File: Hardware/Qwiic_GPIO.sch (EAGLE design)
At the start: 26 parts, among them J2 SMD, J3 PTH, J4 SMD, U3 TCA9534U

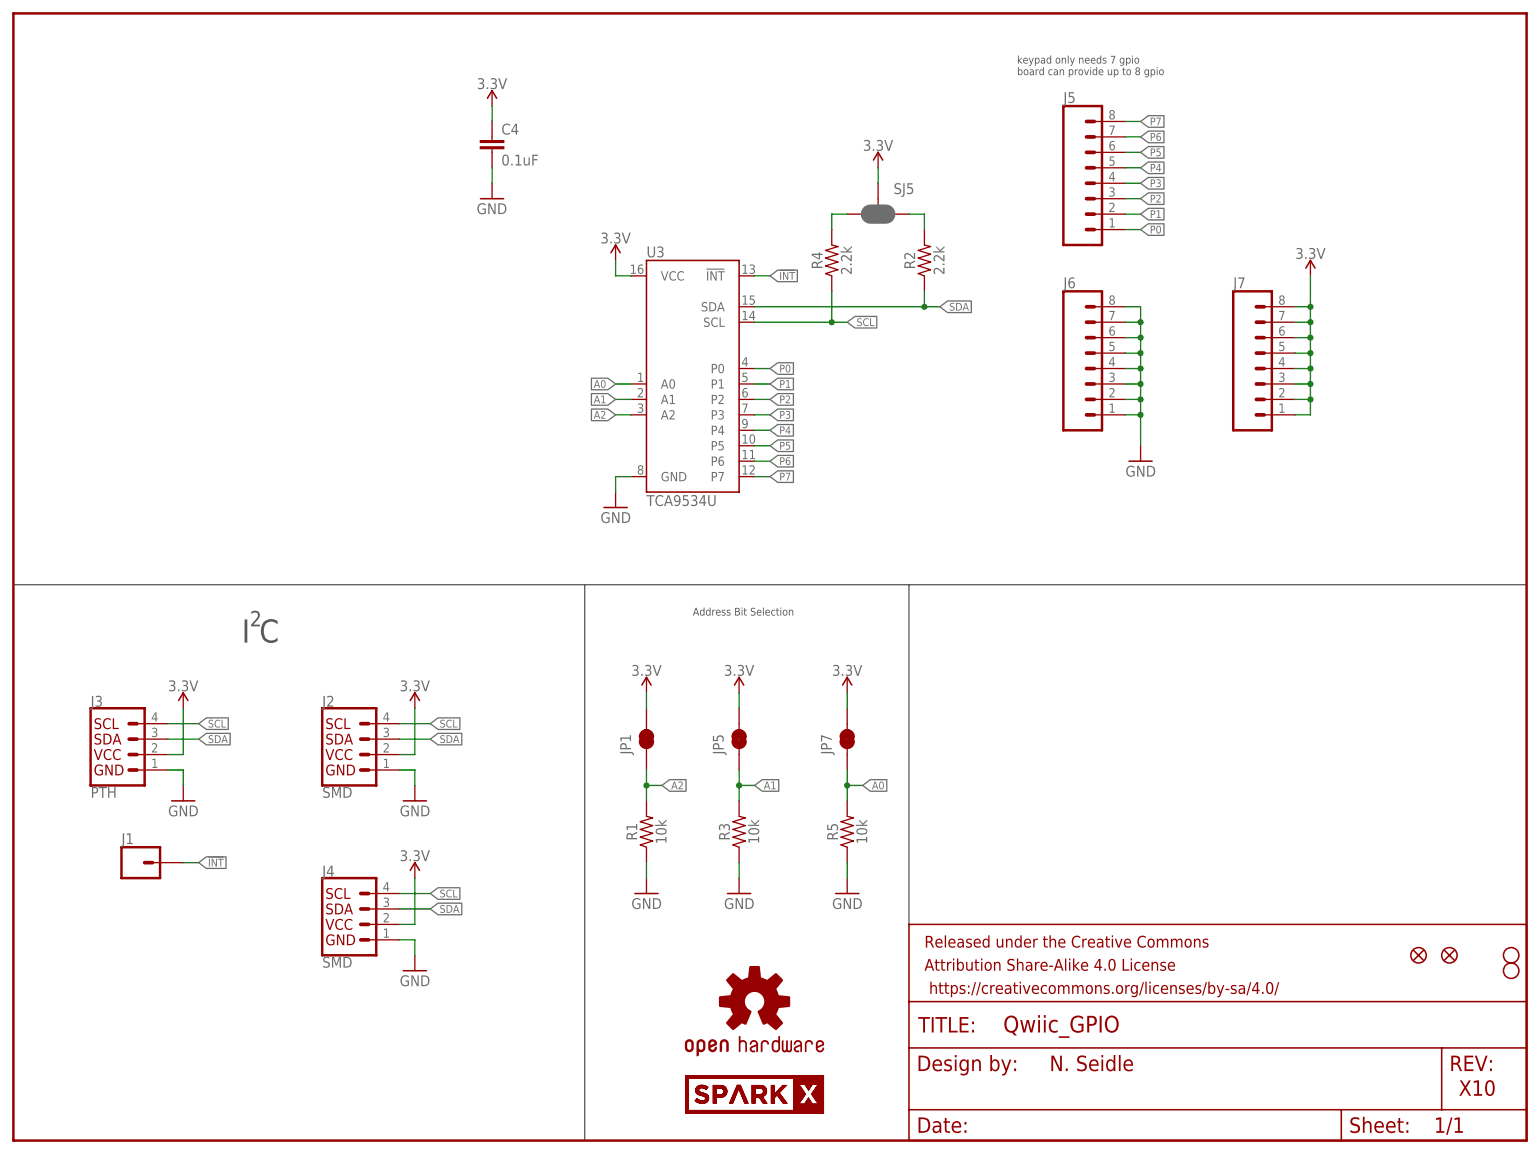
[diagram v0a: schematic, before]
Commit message: added addresses
cleaned up schematic and added addresses.
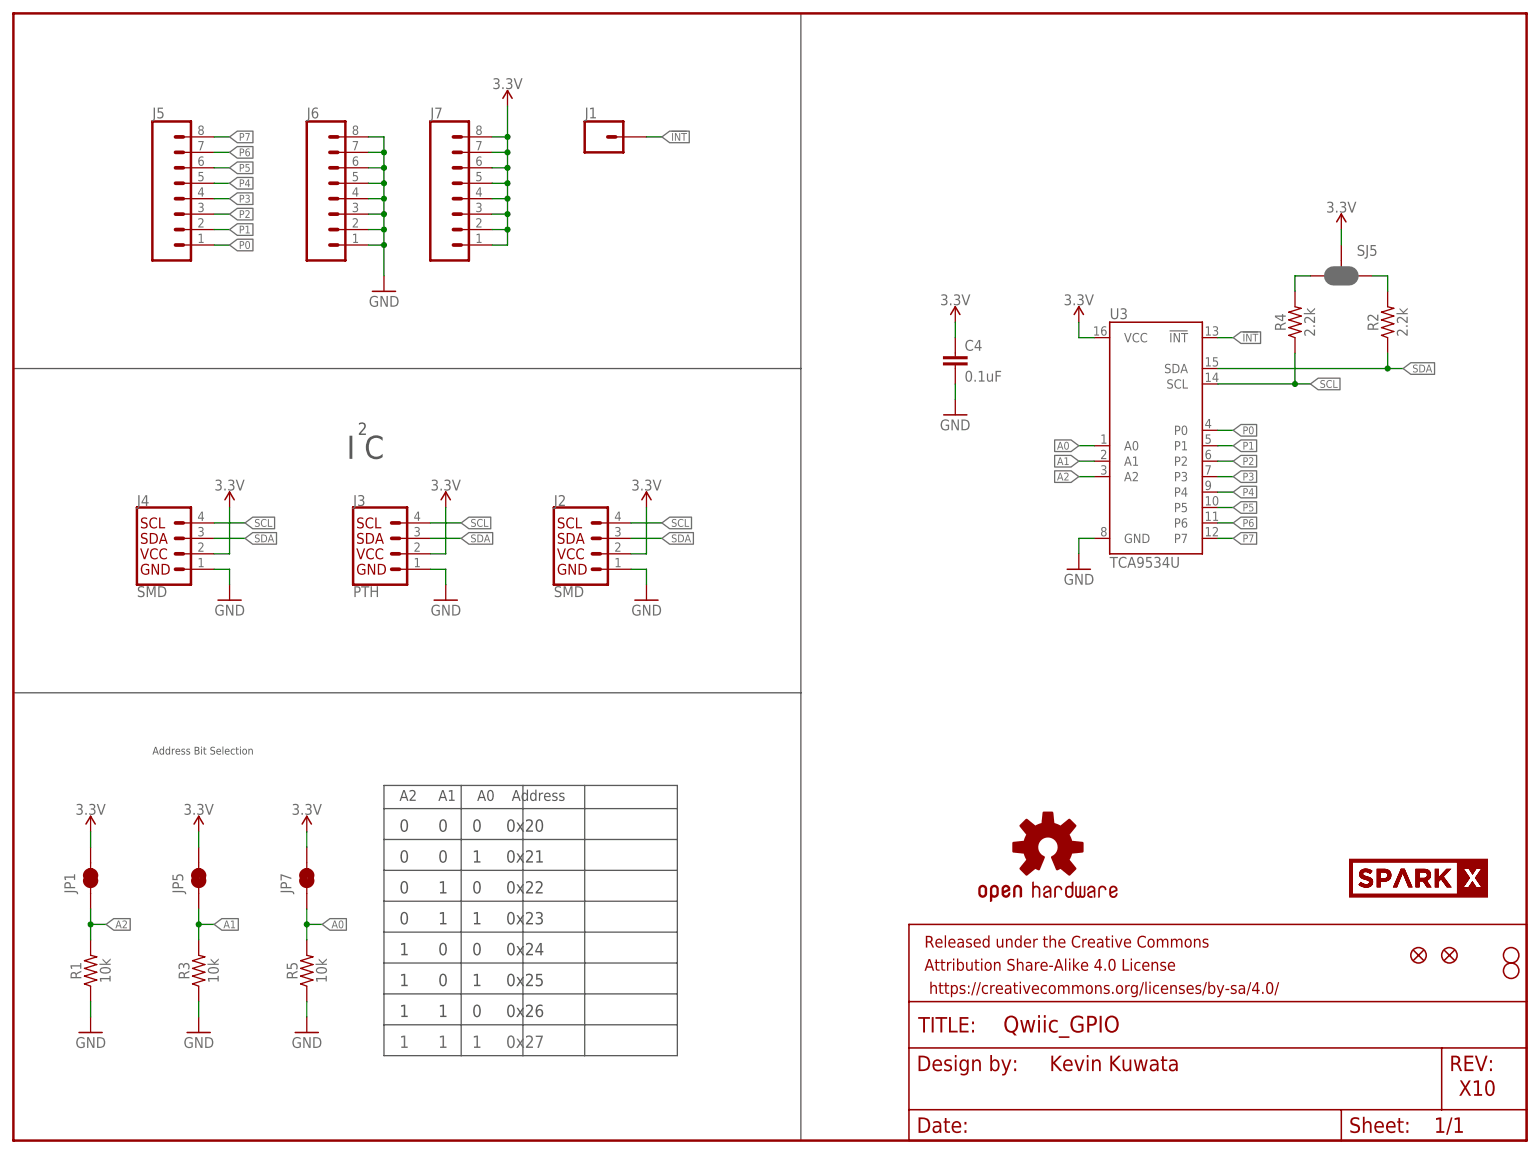
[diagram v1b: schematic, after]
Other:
- note added: "0 0 0 0x20"
- note added: "0 0 1 0x21"
- note added: "0 1 0 0x22"
- note added: "0 1 1 0x23"
- note added: "1 0 0 0x24"
- note added: "1 0 1 0x25"
- note added: "1 1 0 0x26"
- note added: "1 1 1 0x27"
- note added: "A2 A1 A0 Address"
- note added: "Kevin Kuwata"
- note removed: "N. Seidle"
- note removed: "keypad only needs 7 gpio board can provide up to 8 gpio"
- moved on the sheet: C4, J1, J2, J3, J4, J5, J6, J7, JP1, JP5, JP7, R1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

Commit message: Updated PCB with latch terminals and buzzard labels
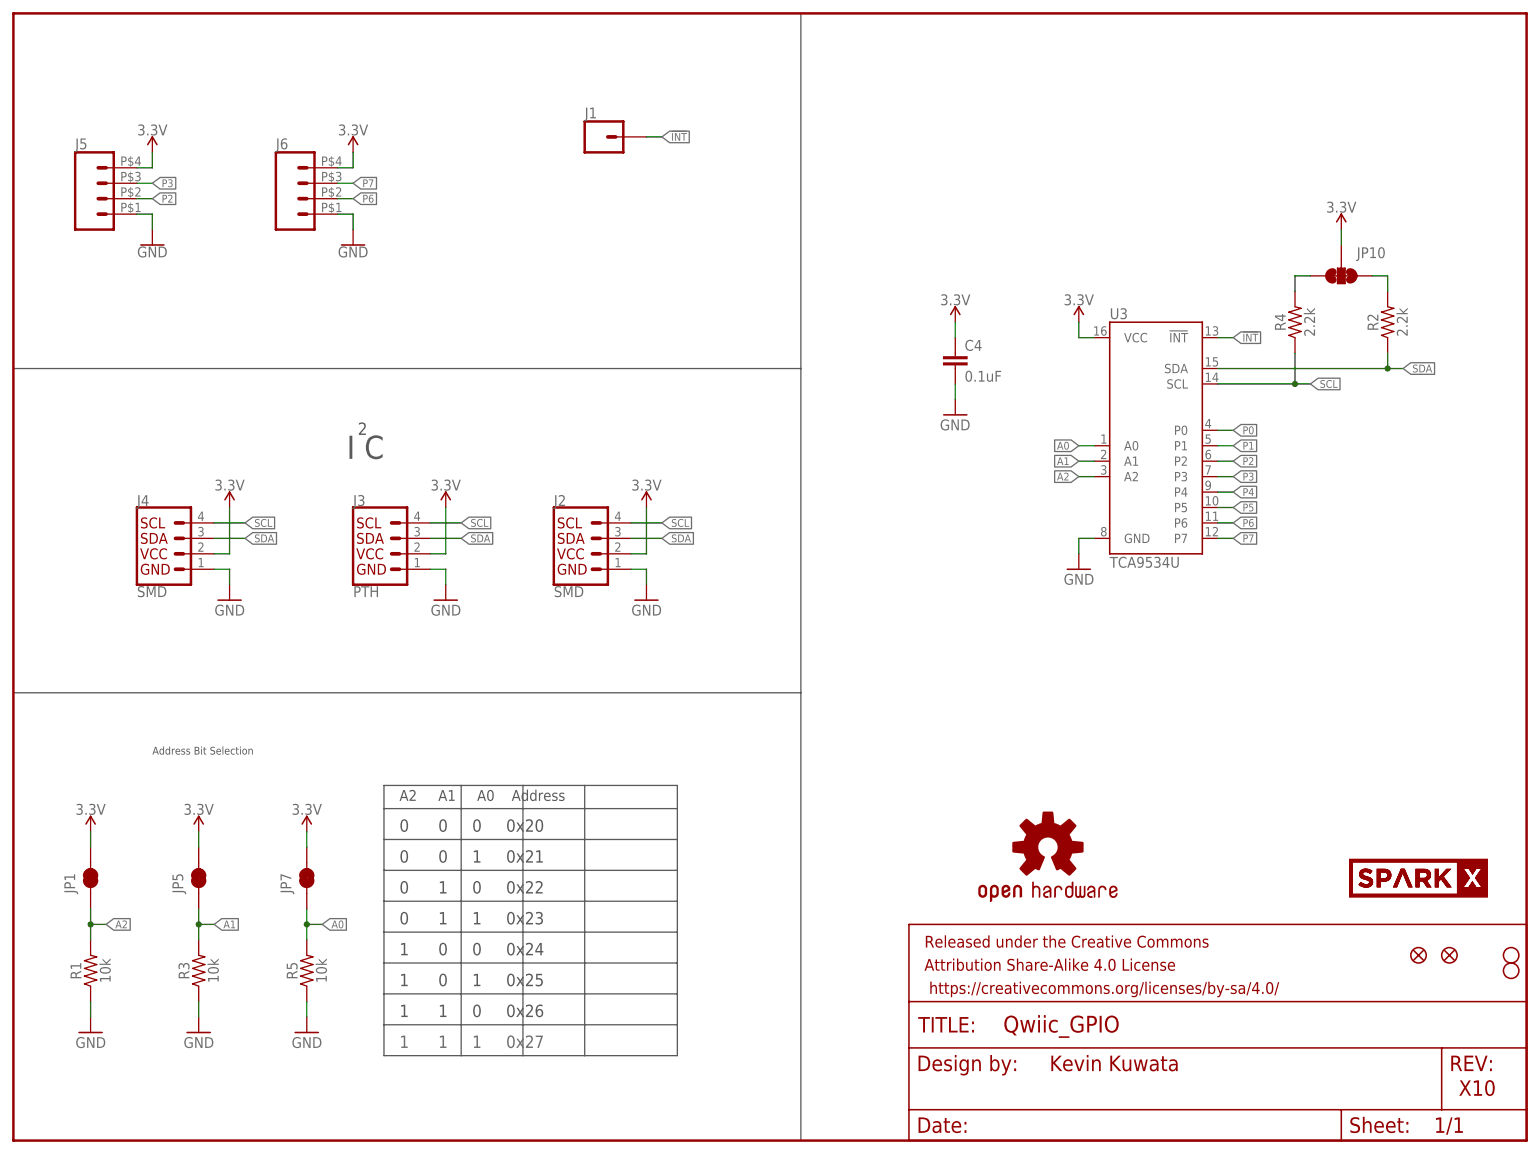
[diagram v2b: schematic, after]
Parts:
- removed J7: (no value), SparkFun-Connectors:CONN_08NO_SILK_FEMALE_PTH
- removed SJ5: SMT-JUMPER-_3-2-NC-PASTE_TALL, KevinKuwata_eagle:SMT-JUMPER-_3-2-NC-PASTE_TALL
- added JP10: JUMPER-SMT_3_2-NC_TRACE_SILK, SparkFun-Jumpers:JUMPER-SMT_3_2-NC_TRACE_SILK
- J5, J6: device SparkFun-Connectors:CONN_08NO_SILK_FEMALE_PTH -> SparkFun-Connectors:CONN_04LATCH
- JP1, JP5, JP7: value JUMPER-SMT_2_NC_TRACE_NO-SILK -> JUMPER-SMT_2_NC_TRACE_SILK; device SparkFun-Jumpers:JUMPER-SMT_2_NC_TRACE_NO-SILK -> SparkFun-Jumpers:JUMPER-SMT_2_NC_TRACE_SILK
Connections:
- net 3.3V: now also J5.4, J6.4, JP10.2; no longer J7.1, J7.2, J7.3, J7.4, J7.5, J7.6, J7.7, J7.8, SJ5.2
- net GND: now also J5.1; no longer J6.2, J6.3, J6.4, J6.5, J6.6, J6.7, J6.8
- net P0: no longer J5.1
- net P1: no longer J5.2
- net P2: now also J5.2; no longer J5.3
- net P3: now also J5.3; no longer J5.4
- net P4: no longer J5.5
- net P5: no longer J5.6
- net P6: now also J6.2; no longer J5.7
- net P7: now also J6.3; no longer J5.8
- net SCL_PU1: now also JP10.1; no longer SJ5.1
- net SDA_PU1: now also JP10.3; no longer SJ5.3

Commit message: Fixed routing and silk issues. Ready to order rev X02
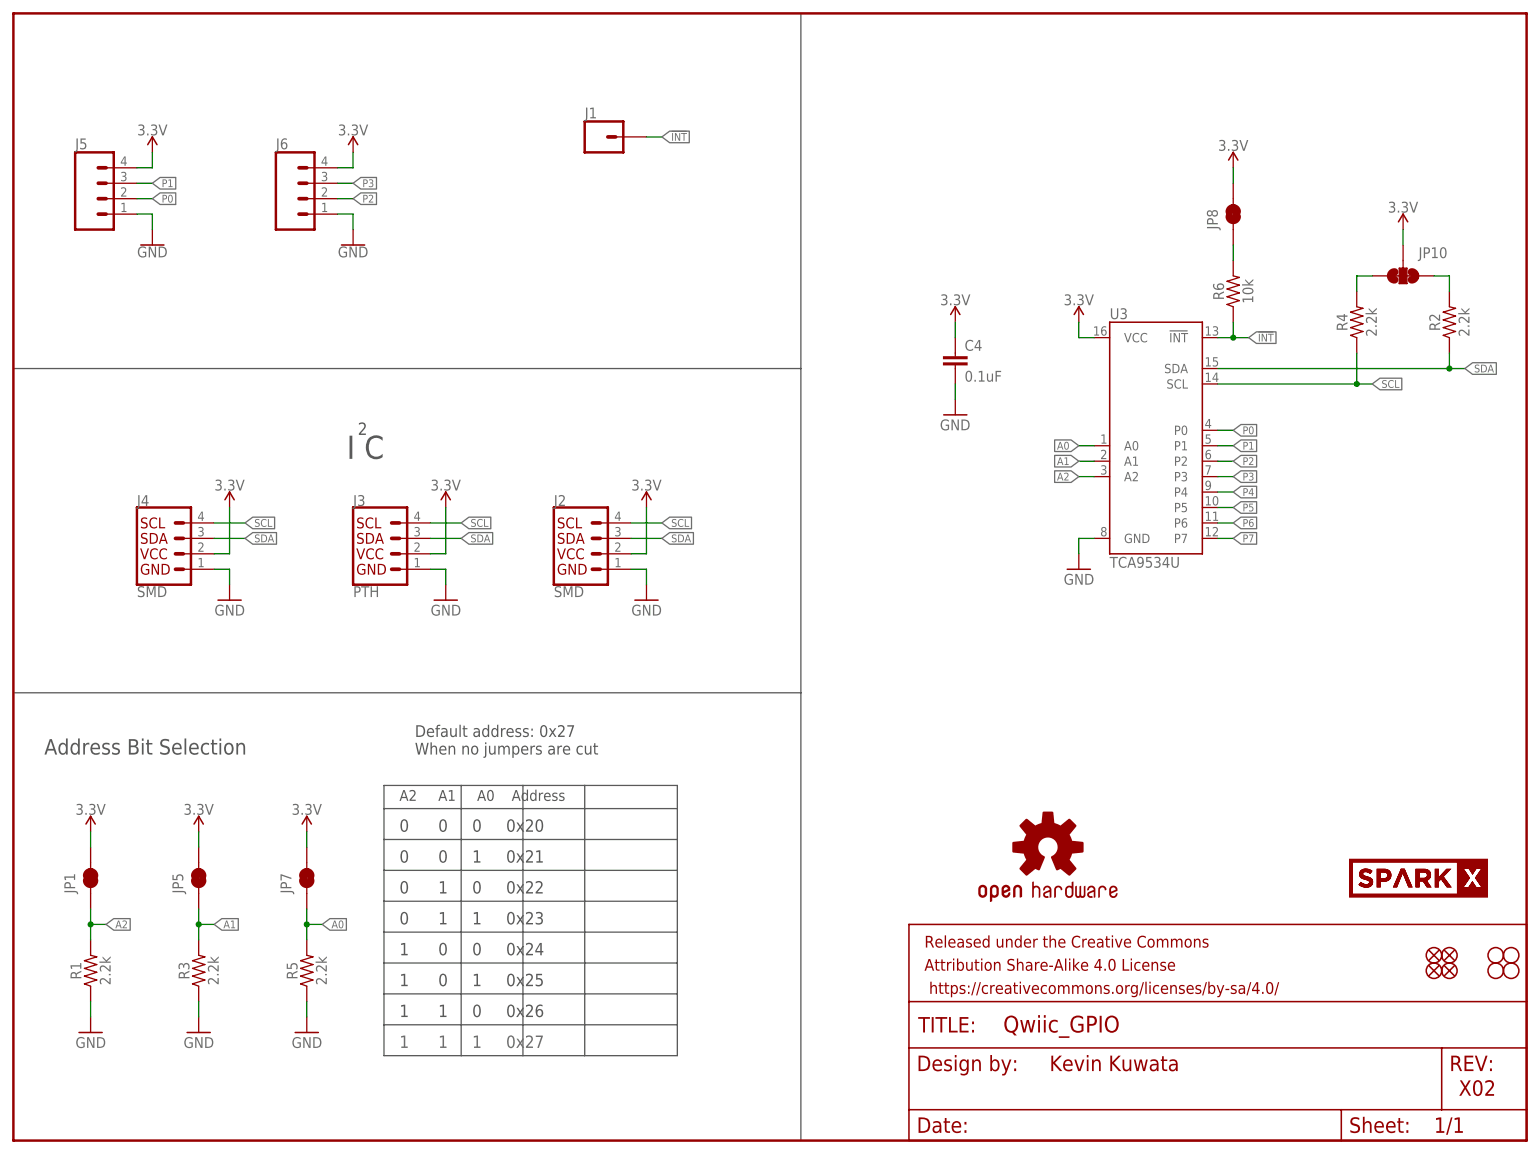
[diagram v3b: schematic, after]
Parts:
- added FD1, FD2: FIDUCIAL1X2, SparkFun-Aesthetics:FIDUCIAL1X2
- added H1, H2: STAND-OFF, SparkFun-Hardware:STAND-OFF
- added JP8: JUMPER-SMT_2_NC_TRACE_SILK, SparkFun-Jumpers:JUMPER-SMT_2_NC_TRACE_SILK
- added R6: 10k, SparkFun-Resistors:10KOHM-0603-1/10W-1%
- JP2, JP6: value FIDUCIALUFIDUCIAL -> FIDUCIAL1X2; device SparkFun:FIDUCIALUFIDUCIAL -> SparkFun:FIDUCIAL1X2
- R1, R3, R5: value 10k -> 2.2k
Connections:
- new net N$1: JP8.1, R6.2
- net !INT: now also R6.1
- net 3.3V: now also JP8.2
- net P0: now also J5.2
- net P1: now also J5.3
- net P2: now also J6.2; no longer J5.2
- net P3: now also J6.3; no longer J5.3
- net P6: no longer J6.2
- net P7: no longer J6.3
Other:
- note added: "Default address: 0x27 When no jumpers are cut"
- note added: "X02"
- note removed: "X10"
- moved on the sheet: J5, J6, JP10, R2, R4
